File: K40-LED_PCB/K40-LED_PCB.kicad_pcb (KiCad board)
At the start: 2 copper layers, 26.5 x 61.5 mm, 29 parts, among them U1 LDD_350HS, U2 LM3466, U3 LM3466, U4 LM3466, U5 LM3466, p1 12V_Pad

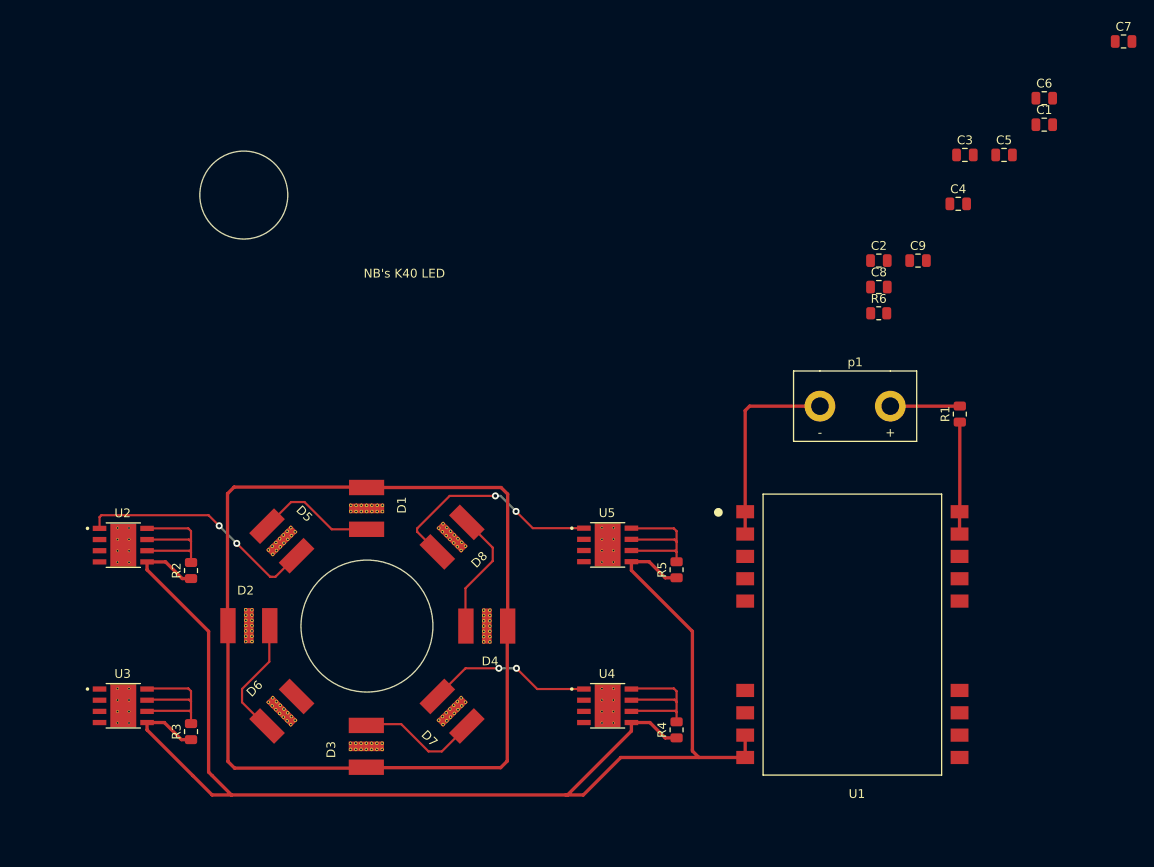
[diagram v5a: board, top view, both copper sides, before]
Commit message: PCB_Updates_Chaned_LM_Layout
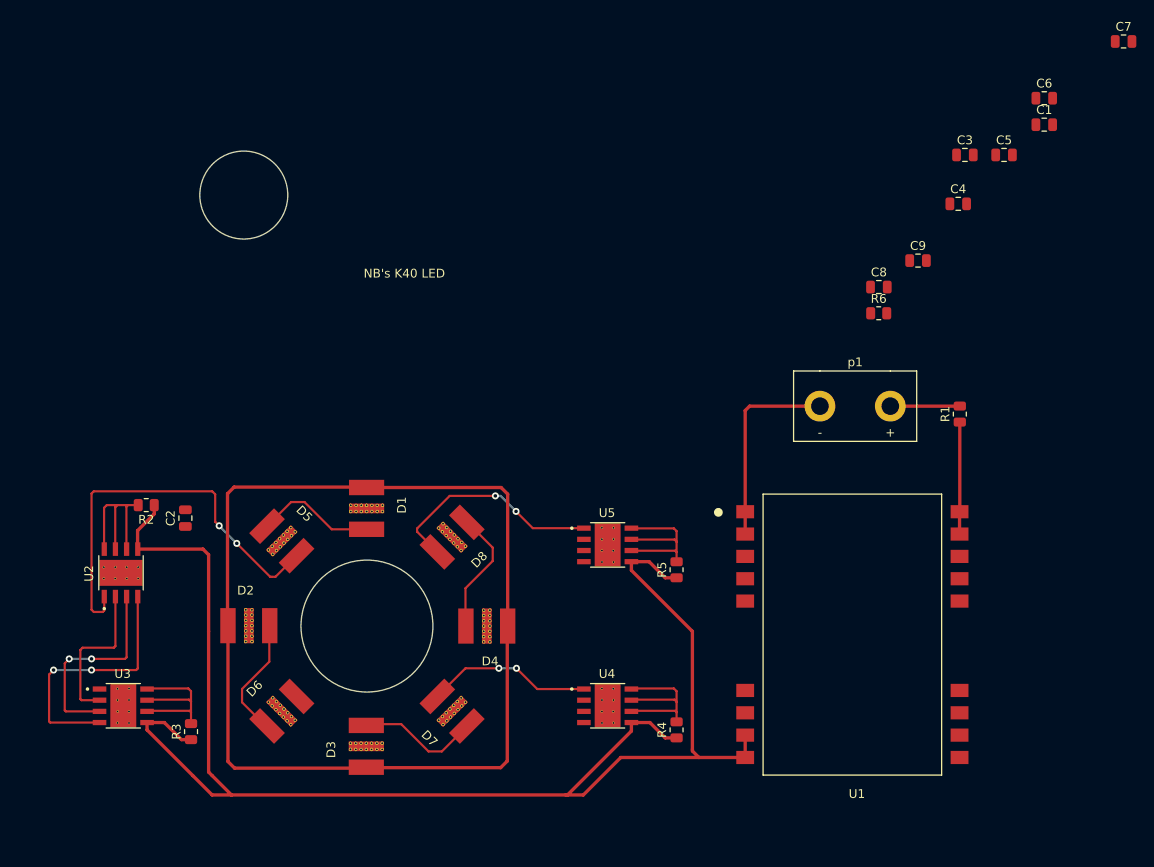
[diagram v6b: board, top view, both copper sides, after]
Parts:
- moved C2 84.1 mm to (70.4, 109.7), turned to 90 degrees
- moved R2 9.01 mm to (65.9, 108.2), turned to 180 degrees
- moved U2 3.16 mm to (63.0, 116.0), turned to 90 degrees
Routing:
- net Net-(R6-Pad2): track 0.00 -> 29.7 mm, vias 0 -> 2
- net Net-(C1-Pad1): track 125.4 -> 149.0 mm, vias 0 -> 2
- net Net-(C2-Pad1): track 27.7 -> 46.7 mm
- net Net-(U2-Pad2): track 0.00 -> 17.6 mm
- net GND: track 166.7 -> 172.9 mm
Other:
- net class Default removed

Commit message: Finished_PCB
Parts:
- moved C3 122.0 mm to (58.2, 137.2)
- moved C1 114.6 mm to (69.8, 124.0)
- moved C4 103.3 mm to (69.8, 127.2)
- moved C7 86.2 mm to (124.7, 124.0)
- moved C5 85.2 mm to (113.2, 137.2)
- moved C6 78.3 mm to (124.8, 127.2)
- moved C9 45.4 mm to (125.8, 116.2), turned to -90 degrees
- moved C8 44.8 mm to (124.7, 121.0)
- moved R6 39.7 mm to (123.0, 116.2), turned to -90 degrees
- moved C2 11.3 mm to (69.8, 121.0), turned to 0 degrees
- moved R5 9.06 mm to (120.9, 108.2), turned to 180 degrees
- moved U5 3.31 mm to (118.1, 116.1), turned to 90 degrees
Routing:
- net Net-(C1-Pad1): track 149.0 -> 292.0 mm, vias 2 -> 18
- net Net-(U2-Pad2): track 17.6 -> 136.1 mm, vias 0 -> 2
- net Net-(R6-Pad2): track 29.7 -> 135.7 mm, vias 2 -> 6
- net GND: track 172.9 -> 217.5 mm
- net Net-(C4-Pad1): track 0.00 -> 27.0 mm, vias 0 -> 2
- net Net-(C8-Pad1): track 25.6 -> 47.0 mm, vias 2 -> 4
- net Net-(C6-Pad1): track 19.0 -> 28.3 mm
- net Net-(C2-Pad1): track 46.7 -> 53.1 mm, vias 2 -> 4
- net Net-(C9-Pad1): track 0.00 -> 2.77 mm
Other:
- board size 26.5 x 61.5 mm -> 111.8 x 58.4 mm

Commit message: Lots of updates on the K40 LED
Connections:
- U4 pad 9: (no net) -> GND
- U5 pad 9: (no net) -> GND
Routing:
- net GND: track 217.5 -> 224.5 mm
- added copper zone on B.Cu, net GND
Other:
- outline, holes or cut-outs redrawn
